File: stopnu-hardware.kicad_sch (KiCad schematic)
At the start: 17 parts, among them CN1 SM04B-SRSS-TB (LF)(SN), CN2 OQ0232510000G, CN3 OQ0232510000G, CN4 OQ0232510000G, CN5 OQ0232510000G, CN6 OQ0432510000G, J1 Conn_02x15_Odd_Even

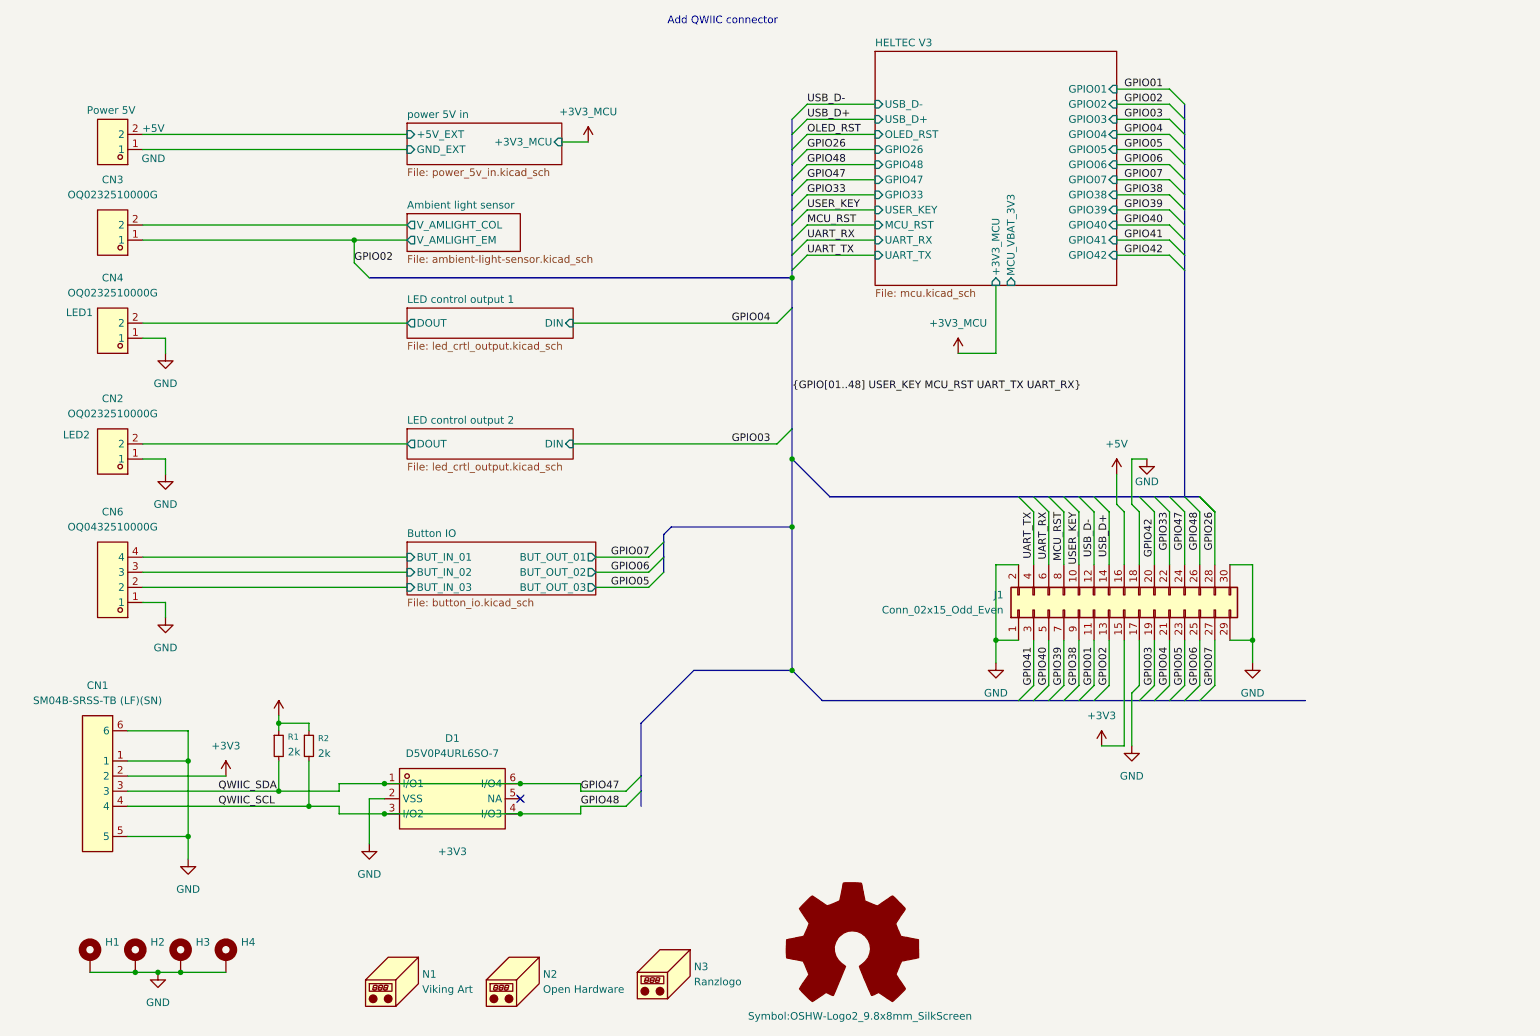
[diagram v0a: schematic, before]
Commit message: Fixed some pinout issues.
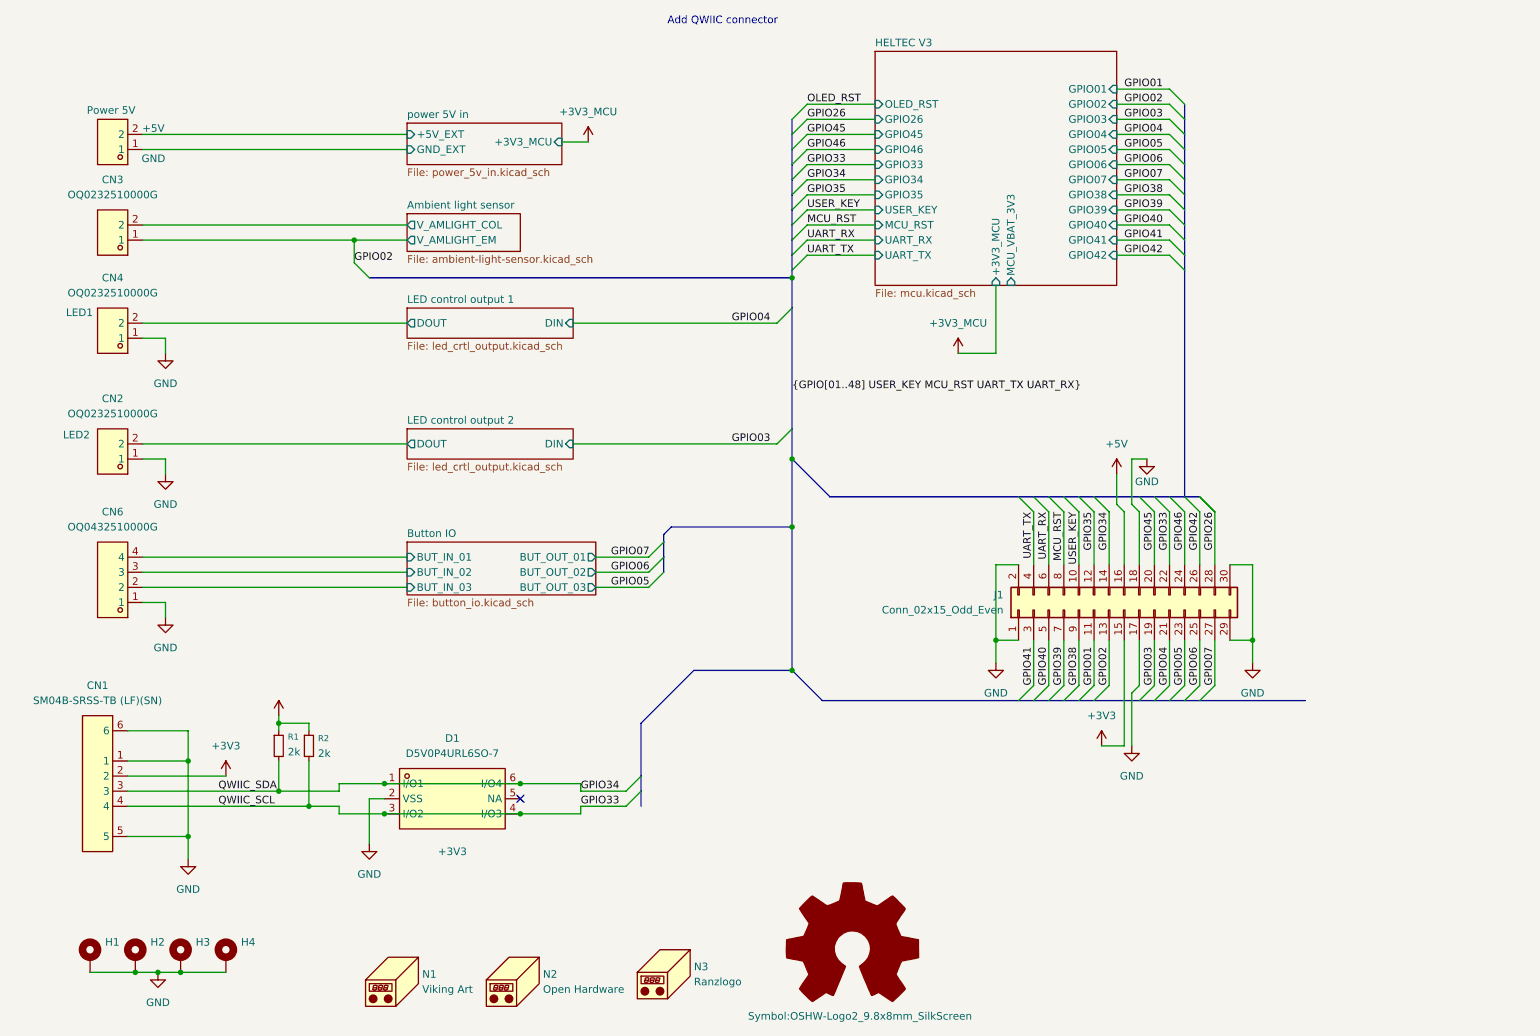
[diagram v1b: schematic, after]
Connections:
- net USB_D+ is gone; now on net GPIO34: J1.14 (Pin_14)
- net GPIO33: now also CN1.4, D1.3 (I/O2), D1.4 (I/O3), R2.2
- net GPIO42: now also J1.26 (Pin_26); no longer J1.20 (Pin_20)
- net GPIO47 renamed GPIO34
- net GPIO34: no longer J1.24 (Pin_24)
- removed net GPIO48: CN1.4, D1.3 (I/O2), D1.4 (I/O3), J1.26 (Pin_26), R2.2
- net USB_D- renamed GPIO35
- new net GPIO45: J1.20 (Pin_20)
- new net GPIO46: J1.24 (Pin_24)
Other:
- sheet HELTEC V3 ports: added GPIO34, GPIO35, GPIO45, GPIO46; removed GPIO47, GPIO48, USB_D+, USB_D-
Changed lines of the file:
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@@
 	)
 	(bus_entry
-		(at 142.24 39.37)
+		(at 142.24 52.07)
 		(size 2.54 -2.54)
 		(stroke
@@
 	)
 	(bus_entry
-		(at 142.24 41.91)
+		(at 142.24 36.83)
 		(size 2.54 -2.54)
 		(stroke
@@
 	)
 	(bus_entry
-		(at 142.24 46.99)
+		(at 142.24 41.91)
 		(size 2.54 -2.54)
 		(stroke
@@
 	)
 	(bus_entry
-		(at 142.24 36.83)
+		(at 142.24 49.53)
 		(size 2.54 -2.54)
 		(stroke
@@
 	)
 	(bus_entry
-		(at 142.24 44.45)
+		(at 142.24 39.37)
 		(size 2.54 -2.54)
 		(stroke
@@
 	)
 	(bus_entry
-		(at 142.24 49.53)
+		(at 142.24 44.45)
 		(size 2.54 -2.54)
 		(stroke
@@
 	)
 	(bus_entry
-		(at 142.24 52.07)
+		(at 142.24 46.99)
 		(size 2.54 -2.54)
 		(stroke
@@
 	(wire
 		(pts
-			(xy 144.78 36.83) (xy 156.21 36.83)
+			(xy 144.78 49.53) (xy 156.21 49.53)
 		)
 		(stroke
@@
 		)
 	)
-	(bus
-		(pts
-			(xy 142.24 36.83) (xy 142.24 39.37)
-		)
-		(stroke
-			(width 0)
-			(type default)
-		)
-	)
 	(wire
 		(pts
@@
 	(wire
 		(pts
-			(xy 203.2 102.87) (xy 203.2 111.76)
-		)
-		(stroke
-			(width 0)
-			(type default)
-		)
-	)
-	(wire
-		(pts
 			(xy 60.96 138.43) (xy 60.96 139.7)
 		)
@@
 	(wire
 		(pts
-			(xy 144.78 49.53) (xy 156.21 49.53)
+			(xy 144.78 44.45) (xy 156.21 44.45)
 		)
 		(stroke
@@
 	(wire
 		(pts
+			(xy 203.2 102.87) (xy 203.2 111.76)
+		)
+		(stroke
+			(width 0)
+			(type default)
+		)
+	)
+	(wire
+		(pts
 			(xy 33.02 73.66) (xy 36.83 73.66)
 		)
@@
 	(wire
 		(pts
-			(xy 144.78 46.99) (xy 156.21 46.99)
+			(xy 144.78 41.91) (xy 156.21 41.91)
 		)
 		(stroke
@@
 		)
 	)
+	(bus
+		(pts
+			(xy 142.24 46.99) (xy 142.24 49.53)
+		)
+		(stroke
+			(width 0)
+			(type default)
+		)
+	)
 	(wire
 		(pts
@@
 	(bus
 		(pts
-			(xy 142.24 41.91) (xy 142.24 44.45)
+			(xy 142.24 36.83) (xy 142.24 39.37)
 		)
 		(stroke
@@
 	(wire
 		(pts
-			(xy 144.78 34.29) (xy 156.21 34.29)
+			(xy 144.78 46.99) (xy 156.21 46.99)
 		)
 		(stroke
@@
 		)
 	)
+	(bus
+		(pts
+			(xy 142.24 49.53) (xy 142.24 52.07)
+		)
+		(stroke
+			(width 0)
+			(type default)
+		)
+	)
 	(wire
 		(pts
@@
 	(bus
 		(pts
-			(xy 142.24 44.45) (xy 142.24 46.99)
+			(xy 142.24 39.37) (xy 142.24 41.91)
 		)
 		(stroke
@@
 	(wire
 		(pts
-			(xy 144.78 44.45) (xy 156.21 44.45)
+			(xy 144.78 39.37) (xy 156.21 39.37)
 		)
 		(stroke
@@
 		)
 	)
-	(bus
-		(pts
-			(xy 142.24 39.37) (xy 142.24 41.91)
-		)
-		(stroke
-			(width 0)
-			(type default)
-		)
-	)
 	(wire
 		(pts
@@
 	(wire
 		(pts
-			(xy 144.78 41.91) (xy 156.21 41.91)
+			(xy 144.78 36.83) (xy 156.21 36.83)
 		)
 		(stroke
@@
 	(bus
 		(pts
-			(xy 142.24 46.99) (xy 142.24 49.53)
+			(xy 142.24 41.91) (xy 142.24 44.45)
 		)
 		(stroke
@@
 	(bus
 		(pts
-			(xy 142.24 49.53) (xy 142.24 52.07)
+			(xy 142.24 44.45) (xy 142.24 46.99)
 		)
 		(stroke
@@
 	(wire
 		(pts
-			(xy 144.78 39.37) (xy 156.21 39.37)
+			(xy 144.78 34.29) (xy 156.21 34.29)
 		)
 		(stroke
@@
 		)
 	)
-	(label "USB_D+"
-		(at 144.78 36.83 0)
+	(label "GPIO35"
+		(at 144.78 49.53 0)
 		(effects
 			(font
@@
 		)
 	)
-	(label "GPIO47"
+	(label "GPIO34"
 		(at 106.68 149.86 0)
 		(effects
@@
 	)
 	(label "GPIO26"
-		(at 144.78 41.91 0)
+		(at 144.78 36.83 0)
 		(effects
 			(font
@@
 	)
 	(label "GPIO33"
-		(at 144.78 49.53 0)
+		(at 144.78 44.45 0)
 		(effects
 			(font
@@
 		)
 	)
-	(label "GPIO48"
+	(label "GPIO33"
 		(at 106.68 152.4 0)
 		(effects
@@
 		)
 	)
-	(label "USB_D-"
-		(at 144.78 34.29 0)
+	(label "GPIO34"
+		(at 144.78 46.99 0)
 		(effects
 			(font
@@
 		)
 	)
-	(label "GPIO48"
-		(at 144.78 44.45 0)
+	(label "GPIO45"
+		(at 144.78 39.37 0)
 		(effects
 			(font
@@
 	)
 	(label "OLED_RST"
-		(at 144.78 39.37 0)
+		(at 144.78 34.29 0)
 		(effects
 			(font
@@
 	)
 	(label "GPIO42"
-		(at 203.2 110.49 90)
+		(at 210.82 102.87 270)
 		(effects
 			(font
 				(size 1.27 1.27)
 			)
-			(justify left bottom)
+			(justify right bottom)
 		)
 	)
@@
 		)
 	)
-	(label "GPIO47"
-		(at 208.28 102.87 270)
+	(label "GPIO45"
+		(at 203.2 102.87 270)
 		(effects
 			(font
@@
 		)
 	)
-	(label "GPIO48"
-		(at 210.82 102.87 270)
+	(label "GPIO46"
+		(at 208.28 102.87 270)
 		(effects
 			(font
@@
 		)
 	)
-	(label "GPIO47"
-		(at 144.78 46.99 0)
+	(label "GPIO46"
+		(at 144.78 41.91 0)
 		(effects
 			(font
@@
 		)
 	)
-	(label "USB_D-"
-		(at 193.04 110.49 90)
+	(label "GPIO34"
+		(at 195.58 102.87 270)
 		(effects
 			(font
 				(size 1.27 1.27)
 			)
-			(justify left bottom)
+			(justify right bottom)
 		)
 	)
-	(label "USB_D+"
-		(at 195.58 110.49 90)
+	(label "GPIO35"
+		(at 193.04 102.87 270)
 		(effects
 			(font
 				(size 1.27 1.27)
 			)
-			(justify left bottom)
+			(justify right bottom)
 		)
 	)
@@
 		)
 		(pin "GPIO26" input
-			(at 156.21 41.91 180)
+			(at 156.21 36.83 180)
 			(effects
 				(font
@@
 			)
 		)
-		(pin "GPIO47" input
-			(at 156.21 46.99 180)
+		(pin "OLED_RST" input
+			(at 156.21 34.29 180)
 			(effects
 				(font
@@
 			)
 		)
-		(pin "GPIO48" input
+		(pin "GPIO33" input
 			(at 156.21 44.45 180)
 			(effects
@@
 			)
 		)
-		(pin "OLED_RST" input
-			(at 156.21 39.37 180)
+		(pin "+3V3_MCU" input
+			(at 176.53 64.77 270)
 			(effects
 				(font
@@
 			)
 		)
-		(pin "USB_D+" input
-			(at 156.21 36.83 180)
+		(pin "GPIO34" input
+			(at 156.21 46.99 180)
 			(effects
 				(font
@@
 			)
 		)
-		(pin "USB_D-" input
-			(at 156.21 34.29 180)
+		(pin "GPIO35" input
+			(at 156.21 49.53 180)
 			(effects
 				(font
@@
 			)
 		)
-		(pin "GPIO33" input
-			(at 156.21 49.53 180)
+		(pin "GPIO45" input
+			(at 156.21 39.37 180)
 			(effects
 				(font
@@
 			)
 		)
-		(pin "+3V3_MCU" input
-			(at 176.53 64.77 270)
+		(pin "GPIO46" input
+			(at 156.21 41.91 180)
 			(effects
 				(font
